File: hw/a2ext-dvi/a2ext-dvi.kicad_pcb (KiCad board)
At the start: 2 copper layers, 45 x 45 mm, 13 parts, among them J1 Carrier IDC20, J2 HDMI-SWM-19 / Type A

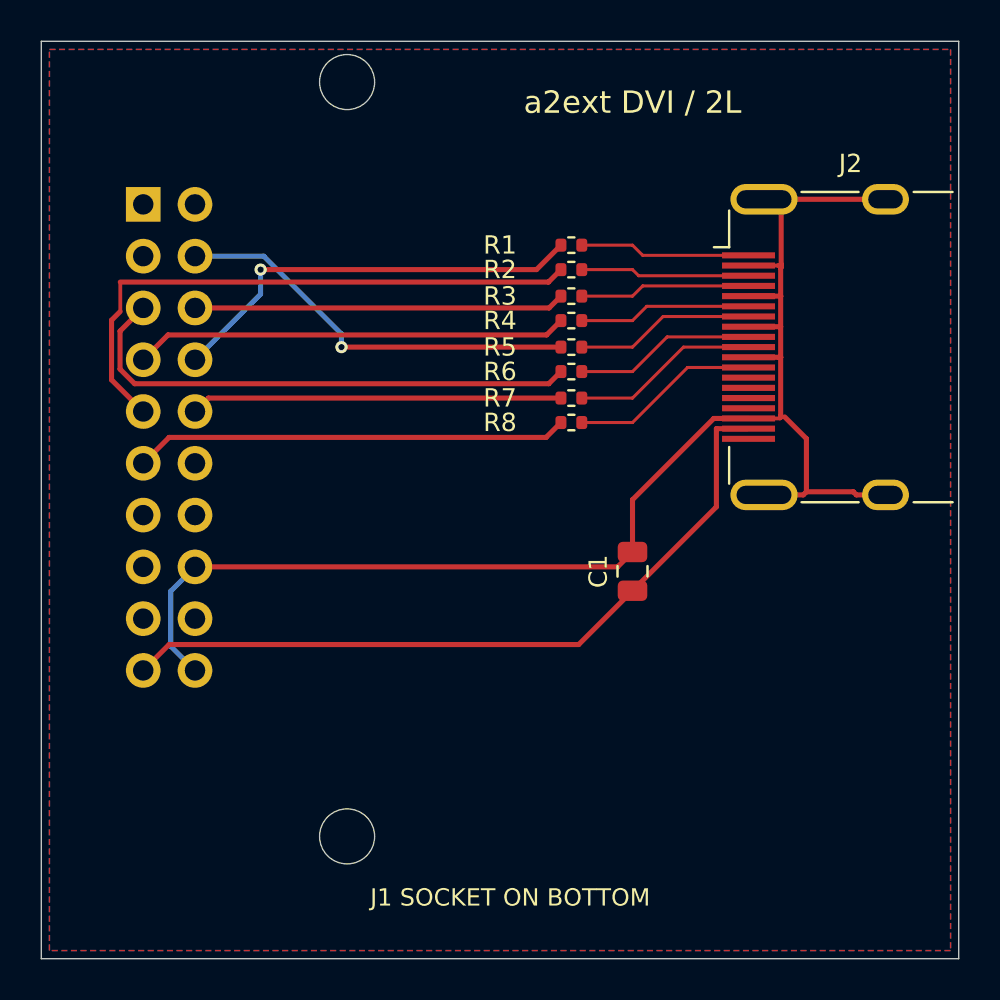
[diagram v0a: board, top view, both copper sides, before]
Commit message: Revise all prototype PCBs for through-hole assembly
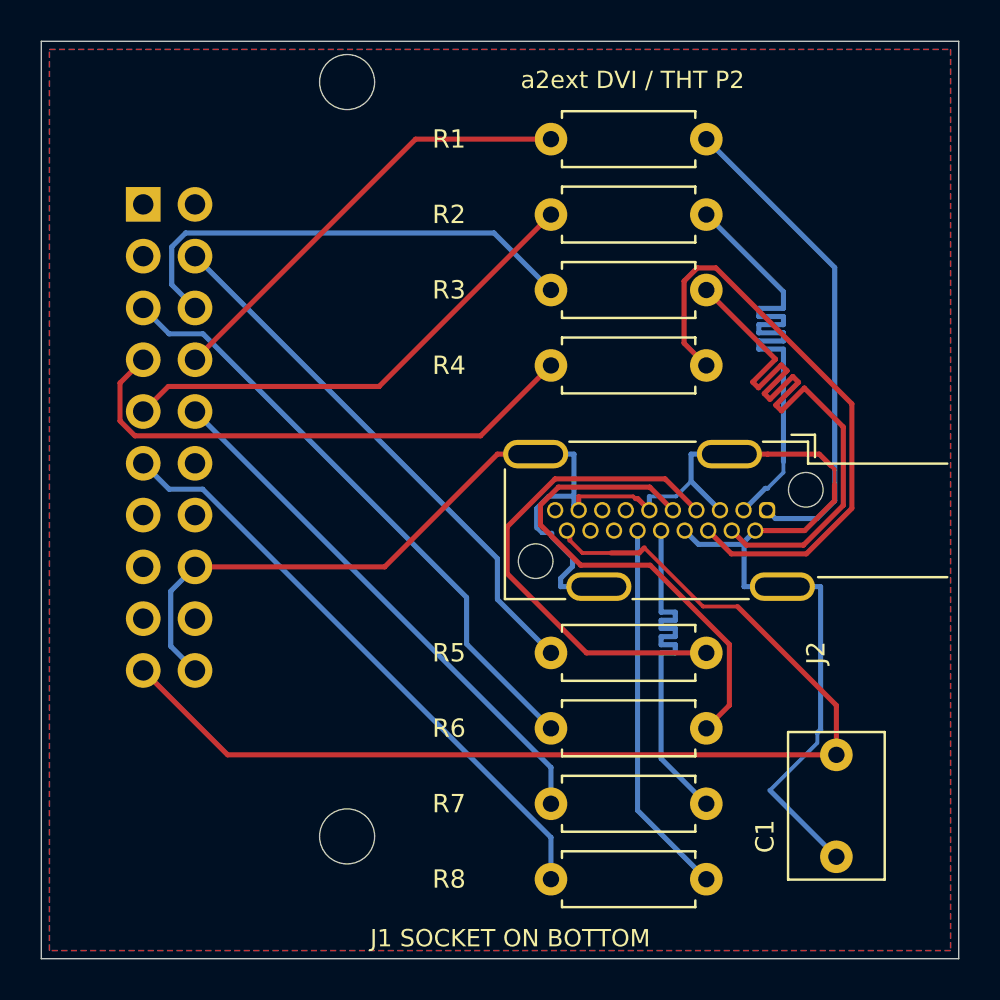
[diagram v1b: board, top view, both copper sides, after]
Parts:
- C1: footprint A2Ext:C0805 -> A2Ext:C_Radial_5
- J2: value HDMI-SWM-19 / Type A -> HDMI Type A THT; footprint A2Ext:HDMI_Molex -> A2Ext:HDMI_Kycon_THT
- R1, R2, R3, R4, R5, R6, R7, R8: footprint A2Ext:R0402 -> A2Ext:R_Axial_7.62
- moved R8 22.4 mm to (90.0, 106.1)
- moved R7 19.9 mm to (90.0, 102.4)
- moved R6 17.5 mm to (90.0, 98.7)
- moved R5 15.0 mm to (90.0, 95.0)
- moved C1 13.5 mm to (104.0, 100.0), turned to -90 degrees
- moved J2 8.35 mm to (100.6, 88.0), turned to -90 degrees
- moved R1 5.30 mm to (90.0, 69.8)
- moved R2 2.88 mm to (90.0, 73.5)
- moved R4 2.42 mm to (90.0, 80.9)
- moved R3 1.04 mm to (90.0, 77.2)
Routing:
- net /TMDS_D1_P: track 8.39 -> 29.4 mm
- net /TMDS_D1_N: track 8.47 -> 29.4 mm
- net /+5V_DB: track 36.9 -> 55.3 mm
- net /TMDS_D2_N: track 8.30 -> 24.2 mm
- net /GND: track 72.7 -> 88.6 mm
- net /TMDS_D2_P: track 8.39 -> 24.2 mm
- net /TMDS_D0_P: track 8.80 -> 24.6 mm
- net /TMDS_D0_N: track 8.88 -> 24.6 mm
- net /TMDS_CLK_P: track 9.22 -> 18.5 mm
- net /TMDS_CLK_N: track 9.30 -> 18.5 mm
- net /CLK_N: track 21.3 -> 29.6 mm
- net /CLK_P: track 18.2 -> 26.5 mm
- net /D0_P: track 20.2 -> 26.7 mm, vias 1 -> 0
- net /D1_P: track 18.2 -> 23.5 mm
- net /D1_N: track 21.3 -> 26.3 mm
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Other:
- board text added: "a2ext DVI / THT P2"
- board text removed: "a2ext DVI / 2L"
